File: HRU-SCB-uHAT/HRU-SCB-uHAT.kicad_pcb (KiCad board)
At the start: 2 copper layers, 67 x 40 mm, 91 parts, among them J1 Conn_01x02_Pin, J2 Conn_01x02_MountingPin, J3 GPIO, J4 GROVE-CONNECTOR-SMD_4+2P-2.0_, J5 GROVE-CONNECTOR-SMD_4+2P-2.0_, J6 Conn_01x03_Pin, U1 MAX14830, U2 74LV1T34GW, U3 SP485EEN, U4 74LV1T34GW, U5 SP485EEN, U6 74LV1T34GW, U7 SP485EEN, U8 74LV1T34GW, U9 SP485EEN, Y1 FA-238 16.0000MB-C3

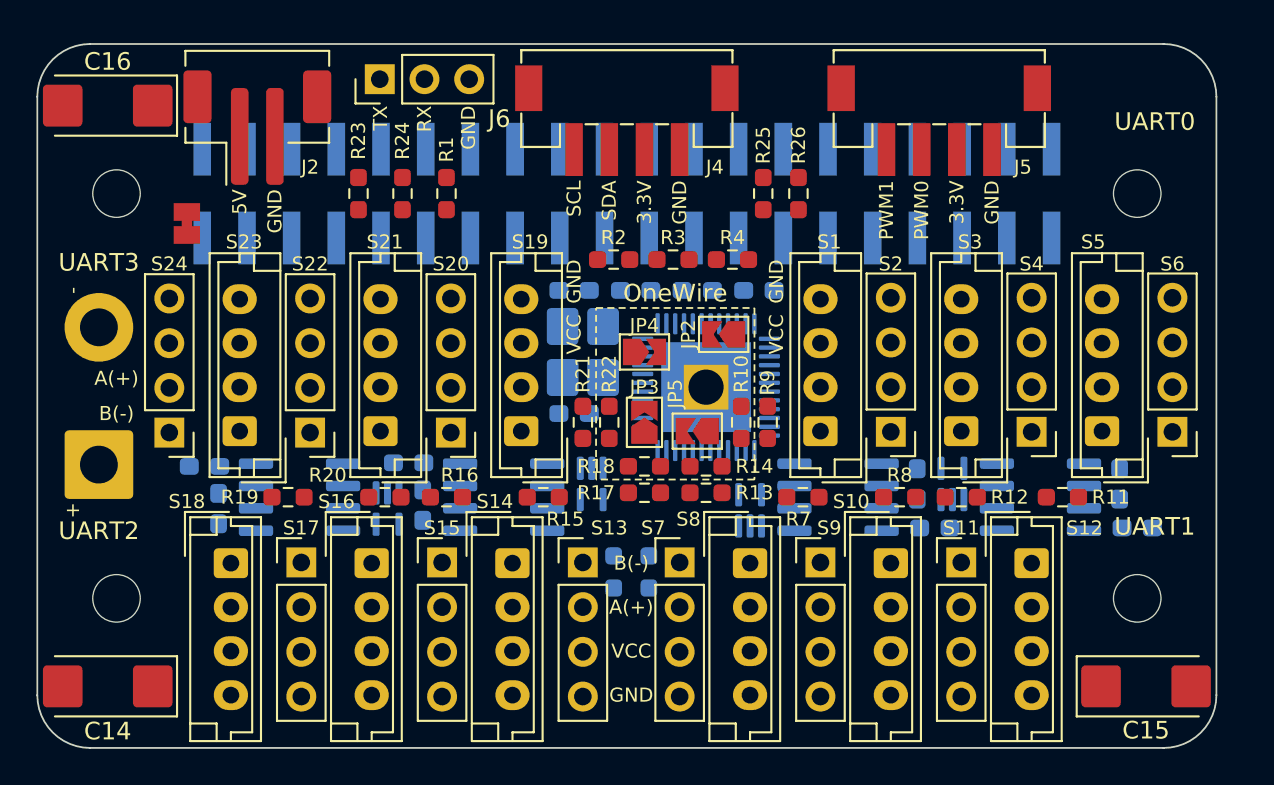
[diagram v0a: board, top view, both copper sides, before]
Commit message: Update: fix ERC error
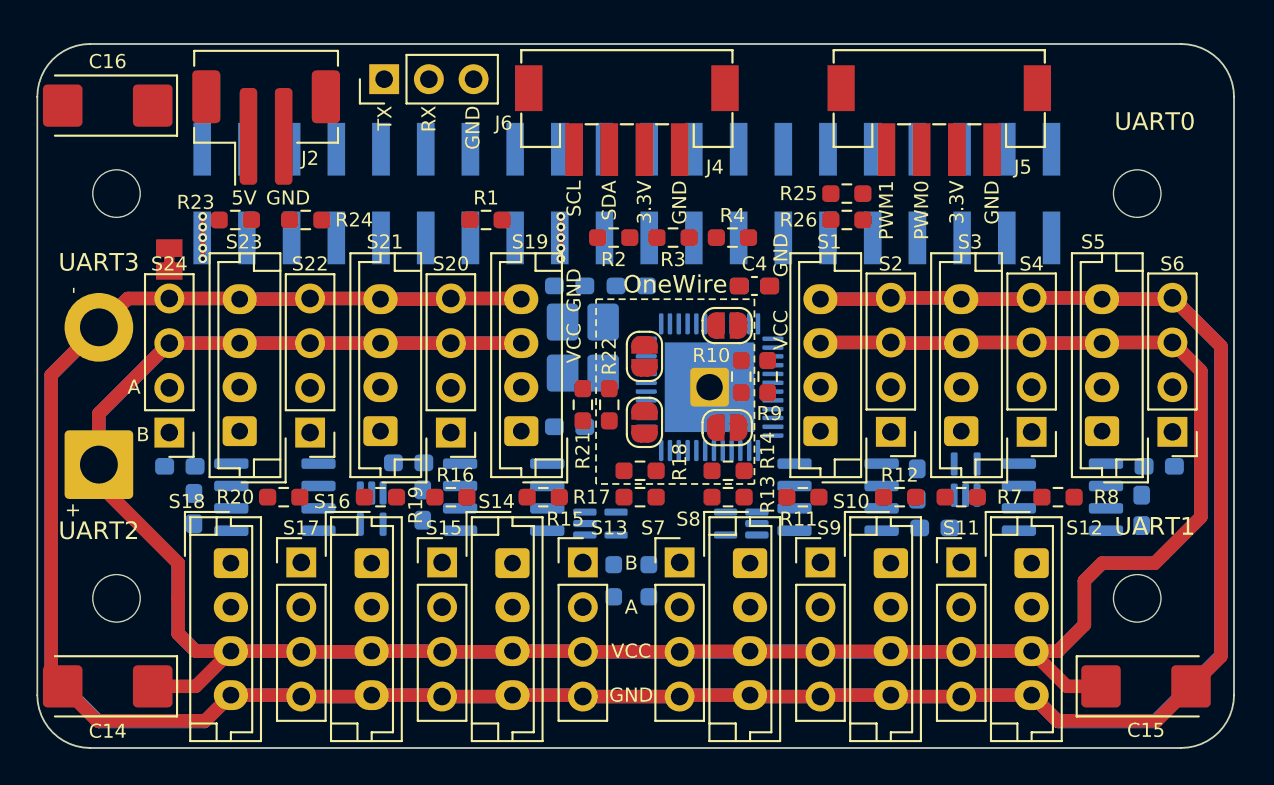
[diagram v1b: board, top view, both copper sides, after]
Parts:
- C4: moved to F.Cu
- JP2, JP3, JP4, JP5: footprint Jumper:SolderJumper-2_P1.3mm_Open_TrianglePad1.0x1.5mm -> Jumper:SolderJumper-2_P1.3mm_Open_RoundedPad1.0x1.5mm
- moved C4 10.3 mm to (139.8, 78.8), turned to 0 degrees
- moved R23 7.16 mm to (110.2, 75.0), turned to 0 degrees
- moved R20 5.75 mm to (113.0, 90.8), turned to 0 degrees
- moved R7 5.75 mm to (151.5, 90.8)
- moved R24 5.70 mm to (114.2, 75.0), turned to 180 degrees
- moved R8 5.50 mm to (157.0, 90.8), turned to 180 degrees
- moved R19 5.25 mm to (118.5, 90.8), turned to 180 degrees
- moved R25 4.75 mm to (145.0, 73.5), turned to 180 degrees
- moved C1 3.76 mm to (132.8, 78.8)
- moved C5 3.76 mm to (129.2, 78.8), turned to 0 degrees
- moved C6 3.72 mm to (162.8, 89.0), turned to 180 degrees
- moved R26 3.13 mm to (145.0, 75.0), turned to 180 degrees
- moved R1 2.70 mm to (124.5, 75.0), turned to 180 degrees
- moved R10 2.60 mm to (139.0, 83.9), turned to 90 degrees
- moved R9 2.60 mm to (140.5, 83.9)
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- renumbered C8 to C6, C9 to C7, C6 to C8, C7 to C9, R7 to R11, R8 to R12, R11 to R7, R12 to R8, U4 to U2, U5 to U3, U2 to U4, U3 to U5
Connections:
- J4 pad 3: +3.3V -> +3V3
- J4 pad 5: GND -> (no net)
- J4 pad 6: GND -> (no net)
- J5 pad 3: +3.3V -> +3V3
- J5 pad 5: GND -> (no net)
- J5 pad 6: GND -> (no net)
- R11 pad 2: /ServoDriver0/SERIAL.RX -> /ServoDriver1/SERIAL.RX
- R23 pad 1: +3.3V -> +3V3
- R24 pad 1: +3.3V -> +3V3
- R7 pad 2: /ServoDriver1/SERIAL.RX -> /ServoDriver0/SERIAL.RX
- U2 pad 4: /ServoDriver1/SERIAL.RX -> /ServoDriver0/SERIAL.RX
- U3 pad 2: /ServoDriver1/SERIAL.~{EN} -> /ServoDriver0/SERIAL.~{EN}
- U3 pad 3: /ServoDriver1/SERIAL.~{EN} -> /ServoDriver0/SERIAL.~{EN}
- U3 pad 4: /ServoDriver1/SERIAL.TX -> /ServoDriver0/SERIAL.TX
- U3 pad 6: /ServoConnector1/SERVO.A -> /ServoConnector0/SERVO.A
- U3 pad 7: /ServoConnector1/SERVO.B -> /ServoConnector0/SERVO.B
- U4 pad 4: /ServoDriver0/SERIAL.RX -> /ServoDriver1/SERIAL.RX
- U5 pad 2: /ServoDriver0/SERIAL.~{EN} -> /ServoDriver1/SERIAL.~{EN}
- U5 pad 3: /ServoDriver0/SERIAL.~{EN} -> /ServoDriver1/SERIAL.~{EN}
- U5 pad 4: /ServoDriver0/SERIAL.TX -> /ServoDriver1/SERIAL.TX
- U5 pad 6: /ServoConnector0/SERVO.A -> /ServoConnector1/SERVO.A
- U5 pad 7: /ServoConnector0/SERVO.B -> /ServoConnector1/SERVO.B
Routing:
- net GNDPWR: track 0.00 -> 315.9 mm
- net VCC: track 0.00 -> 278.1 mm
- net +3V3: track 0.00 -> 7.20 mm, vias 0 -> 10
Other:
- board size 67 x 40 mm -> 68 x 40 mm
- board text added: "A"
- board text added: "B"
- board text removed: "A(+)"
- board text removed: "B(-)"

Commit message: Update: routed wires
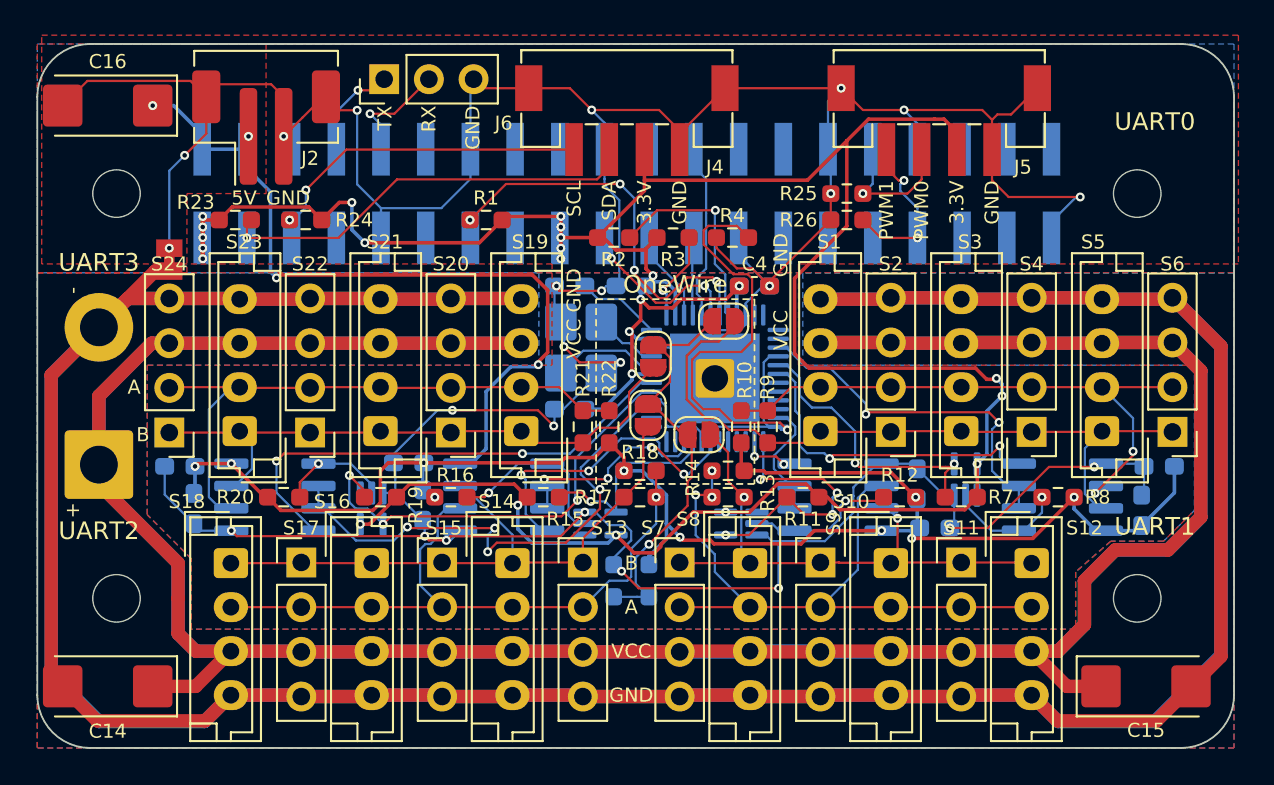
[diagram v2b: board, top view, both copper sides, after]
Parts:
- moved R10 2.85 mm to (139.0, 86.8)
- moved R9 2.85 mm to (140.5, 86.8)
- moved JP3 1.65 mm to (136.6, 87.2)
- moved R21 1.25 mm to (130.0, 86.8)
- moved R22 1.25 mm to (131.5, 86.8)
- moved C3 1.00 mm to (129.2, 85.8)
- moved U1 0.58 mm to (137.5, 84.0)
- moved JP5 0.50 mm to (134.0, 82.8), turned to 90 degrees
- moved JP4 0.45 mm to (133.7, 86.1)
- moved JP2 0.32 mm to (138.0, 80.8)
- moved Y1 0.10 mm to (129.9, 82.2)
- renumbered JP5 to JP3, JP3 to JP4, JP4 to JP5
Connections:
- JP3 pad 1: /ServoConnector3/SERVO.B -> /ServoConnector1/SERVO.B
- JP4 pad 1: /ServoConnector1/SERVO.B -> /ServoConnector2/SERVO.B
- JP5 pad 1: /ServoConnector2/SERVO.B -> /ServoConnector3/SERVO.B
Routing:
- net GND: track 0.15 -> 258.4 mm, vias 0 -> 24
- net +3V3: track 7.20 -> 165.6 mm, vias 10 -> 24
- net +5V: track 0.00 -> 136.3 mm, vias 0 -> 14
- net /ServoConnector0/SERVO.B: track 0.00 -> 40.7 mm
- net /ServoConnector1/SERVO.A: track 0.00 -> 38.9 mm, vias 0 -> 3
- net Net-(U1-~{CTS0}): track 0.00 -> 38.1 mm, vias 0 -> 1
- net /ServoConnector2/SERVO.A: track 0.00 -> 37.8 mm, vias 0 -> 1
- net /ServoConnector2/SERVO.B: track 0.00 -> 35.4 mm
- net /ServoConnector3/SERVO.B: track 0.00 -> 34.5 mm
- net /ServoConnector3/SERVO.A: track 0.00 -> 34.4 mm
- net /ServoConnector0/SERVO.A: track 0.00 -> 34.0 mm, vias 0 -> 2
- net /ServoConnector1/SERVO.B: track 0.00 -> 32.1 mm, vias 0 -> 2
- net /ServoDriver3/SERIAL.~{EN}: track 0.00 -> 29.6 mm, vias 0 -> 4
- net /ServoDriver3/SERIAL.TX: track 0.00 -> 28.2 mm, vias 0 -> 2
- net /ServoDriver3/SERIAL.RX: track 0.00 -> 25.5 mm, vias 0 -> 3
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- added copper zone on F.Cu, net +3V3
- added copper zone on F.Cu, net +5V
- added copper zone on B.Cu, net GND
- added copper zone on B.Cu, net GNDPWR
- added copper zone on F.Cu, net VCC

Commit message: Fix: MAX14830 version
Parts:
- added REF**: Symbol_CC-Attribution_CopperTop_Small, Symbol:Symbol_CC-Attribution_CopperTop_Small, F.Cu at (164.0, 92.2)
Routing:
- net GND: track 258.4 -> 268.2 mm
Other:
- board text added: "CC-BY"
- board text added: "HRU-SCB-uHAT"
